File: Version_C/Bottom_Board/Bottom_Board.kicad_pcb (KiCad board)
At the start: 2 copper layers, 74.8 x 84.5 mm, 47 parts, among them J1 Conn_02x03_Top_Bottom, J2 Conn_02x03_Top_Bottom, J3 Screw_Terminal_01x06, J5 DIN-5, SW2 SW_DIP_x04, U1 LM324, U2 LM324

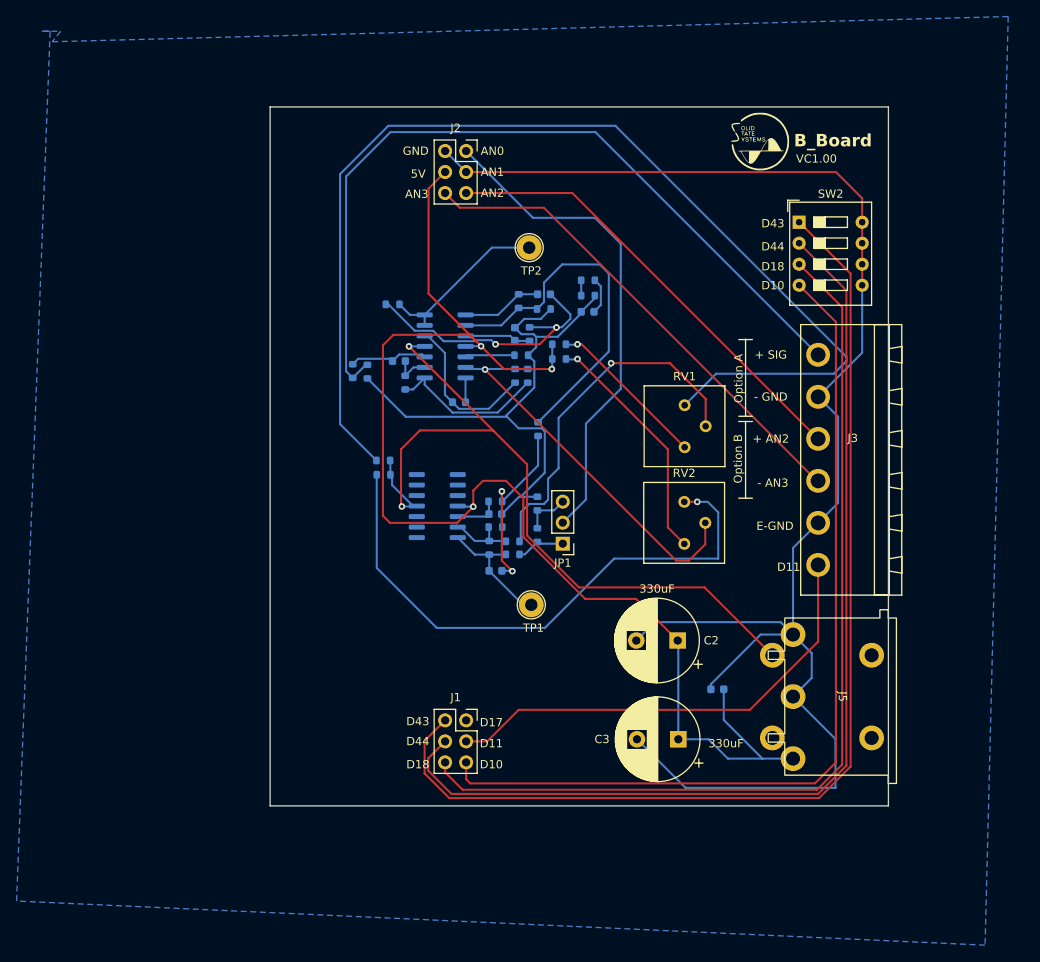
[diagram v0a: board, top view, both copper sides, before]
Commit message: fixed directory overwrite
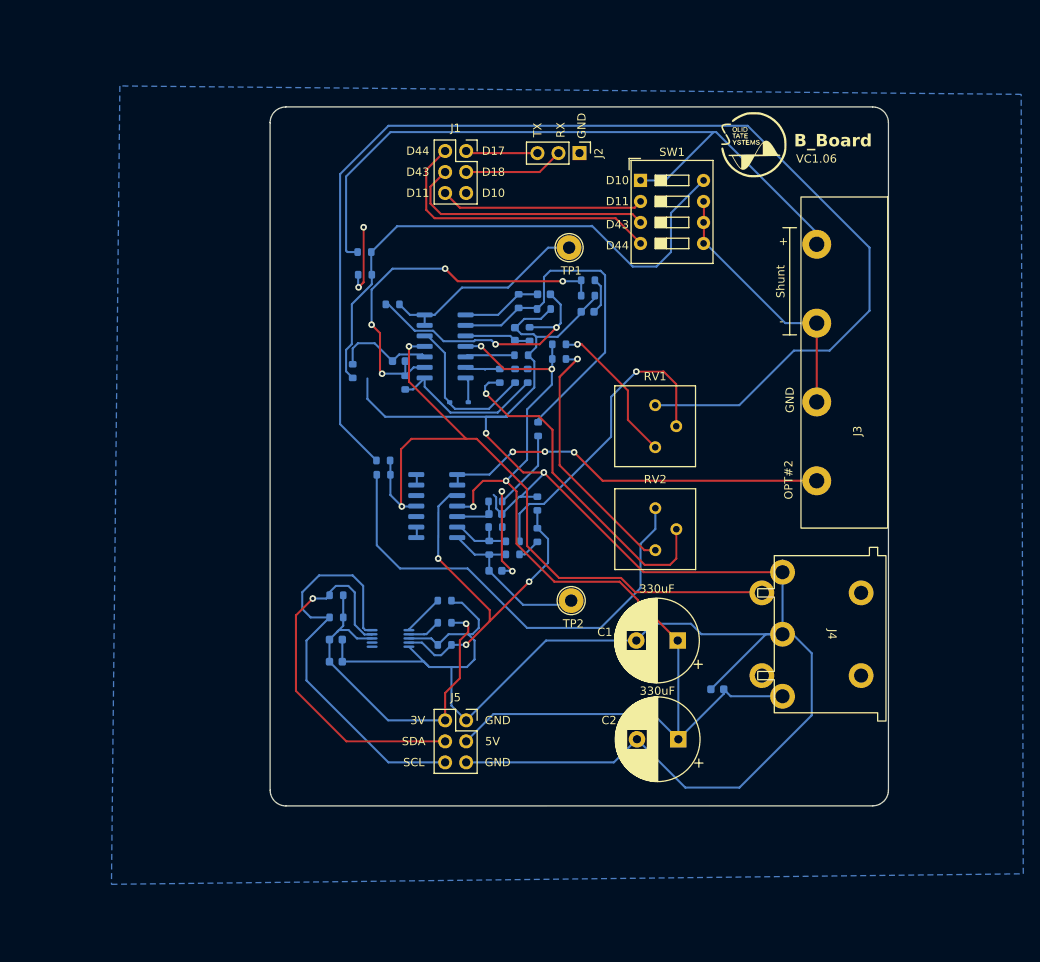
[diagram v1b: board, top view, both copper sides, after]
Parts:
- removed the G*** at (159.3, 67.2)
- removed JP1: Jumper_3_Open, Connector_PinHeader_2.54mm:PinHeader_1x03_P2.54mm_Vertical
- removed the R4 at (111.8, 95.0)
- removed SW2: SW_DIP_x04, Button_Switch_THT:SW_DIP_SPSTx04_Slide_9.78x12.34mm_W7.62mm_P2.54mm
- added C10: 0.1uF, Capacitor_SMD:C_0603_1608Metric, B.Cu at (108.0, 130.1)
- added C9: 1uF, Capacitor_SMD:C_0603_1608Metric, B.Cu at (108.0, 127.4)
- added G***: LOGO, bot_lib:logo_SSS, F.Cu at (158.5, 67.6)
- added G***: LOGO, bot_lib:logo_AN, B.Cu at (104.9, 67.1)
- added J2: Conn_01x03_Pin, Connector_PinHeader_2.54mm:PinHeader_1x03_P2.54mm_Vertical, F.Cu at (137.4, 68.6)
- added R10A1: 20K, Resistor_SMD:R_0603_1608Metric, B.Cu at (111.4, 80.5)
- added R10B1: 20k, Resistor_SMD:R_0603_1608Metric, B.Cu at (111.5, 83.3)
- added R14: 1M, Resistor_SMD:R_0603_1608Metric, B.Cu at (127.8, 95.5)
- added R26: 10K, Resistor_SMD:R_0603_1608Metric, B.Cu at (121.1, 122.7)
- added R27: 10K, Resistor_SMD:R_0603_1608Metric, B.Cu at (108.0, 122.0)
- added R28: 10K, Resistor_SMD:R_0603_1608Metric, B.Cu at (121.1, 125.4)
- added R29: 10K, Resistor_SMD:R_0603_1608Metric, B.Cu at (108.0, 124.7)
- added R30: 3.9M, Resistor_SMD:R_0603_1608Metric, B.Cu at (121.1, 128.0)
- added SW1: SW_DIP_x04, Button_Switch_THT:SW_DIP_SPSTx04_Slide_9.78x12.34mm_W7.62mm_P2.54mm, F.Cu at (144.8, 71.9)
- added U3: ADS1015IDGSR, bot_lib:DGS0010A_N, B.Cu at (114.6, 127.3)
- C11: renamed from C1; value .1uF -> 0.1uF
- C3: renamed from C8; value .1uF -> 0.1uF
- C4: renamed from C7; value 0.1 uF -> 0.1uF
- C5: renamed from C9; value .1uF -> 0.1uF
- C6: renamed from C5; value .002uF -> 0.002uF
- D1: value 1N914 -> 1N4148WS; footprint Diode_SMD:D_0603_1608Metric -> bot_lib:Diode_1N4148WS
- J1: renamed from J2; footprint Connector_PinSocket_2.54mm:PinSocket_2x03_P2.54mm_Vertical -> bot_lib:PinSocket_2x03_P2.54mm_Vertical
- J3: value Screw_Terminal_01x06 -> Screw_Terminal_01x04; footprint Connector_Phoenix_MSTB:PhoenixContact_MSTBA_2,5_6-G-5,08_1x06_P5.08mm_Horizontal -> bot_lib:Terminal_Strip_4_Pin
- J5: renamed from J1; footprint Connector_PinSocket_2.54mm:PinSocket_2x03_P2.54mm_Vertical -> bot_lib:PinSocket_2x03_P2.54mm_Vertical
- RV1, RV2: value 20K -> 20K POT; footprint Potentiometer_THT:Potentiometer_Bourns_3386P_Vertical -> bot_lib:Potentiometer_Bourns_3386P_Vertical
- U1, U2: value LM324 -> LM324DR
- moved J3 10.2 mm to (166.1, 108.2)
- moved J4 7.65 mm to (167.9, 126.7)
- moved TP2 4.85 mm to (136.4, 122.7)
- moved TP1 4.83 mm to (136.1, 80.0)
- moved RV2 3.58 mm to (146.6, 116.6)
- moved RV1 3.56 mm to (146.6, 104.1)
- moved U2 0.06 mm to (120.1, 111.3)
- renumbered C2 to C1, C3 to C2, C6 to C7, C4 to C8, J5 to J4, R10 to R1, R5 to R11, R16 to R12, R19 to R13, R11 to R15, R22 to R16, R3 to R17, R14 to R19, R7 to R2, R1 to R20, R13 to R21, R6 to R22, R9 to R23, R12 to R24, R8 to R25, R24 to R3, R23 to R4, R20 to R5, R2 to R6, R21 to R7, R15 to R8, R17 to R9, TP2 to TP1, TP1 to TP2
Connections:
- net 12V renamed +12V
- net 2x_OUTPUT renamed Net-(R21-Pad2)
- C1 pad 1: 5V -> +5VD
- C1 pad 2: AN1 -> GND
- C11 pad 1: 5V -> +5VD
- C11 pad 2: AN1 -> GND
- C2 pad 1: 5V -> +5VD
- C2 pad 2: AN1 -> GND
- C4 pad 2: E60 -> GND
- C5 pad 2: E60 -> GND
- C7 pad 1: E60 -> GND
- J1 pad 1: AN0 -> TX
- J1 pad 2: AN1 -> D44
- J1 pad 3: AN1 -> RX
- J1 pad 4: 5V -> D43
- J1 pad 5: AN2 -> D10
- J1 pad 6: AN3 -> D11
- J3 pad 1: D11 -> OPT.#2
- J3 pad 2: AN1 -> GND
- J3 pad 3: AN3 -> GND
- J3 pad 4: AN2 -> E23_INPUT
- J4 pad 1: AN1 -> GND
- J4 pad 2: AN1 -> GND
- J4 pad 3: 5V -> +5VD
- J4 pad 6: AN1 -> (no net)
- J4 pad 7: AN1 -> (no net)
- J5 pad 1: D17 -> GND
- J5 pad 2: D43 -> +3V0
- J5 pad 3: D11 -> +5VD
- J5 pad 4: D44 -> SDA
- J5 pad 5: D10 -> GND
- J5 pad 6: D18 -> SCL
- R1 pad 1: Net-(R10-Pad1) -> Net-(U1C--)
- R11 pad 1: E23_INPUT -> SW_OUT
- R19 pad 1: E60 -> GND
- R19 pad 2: 4x_OUTPUT -> AN0
- R2 pad 1: Net-(R10-Pad1) -> Net-(U1C--)
- R2 pad 2: E60 -> GND
- R21 pad 1: 4x_OUTPUT -> AN0
- R23 pad 1: E60 -> GND
- R3 pad 2: E60 -> GND
- R6 pad 2: 5V -> +5VD
- R8 pad 1: 5V -> +5VD
- R9 pad 2: E60 -> GND
- RV2 pad 2: Net-(U1B--) -> Net-(R14-Pad2)
- U1 pad 4: 5V -> +5VD
- U2 pad 1: (no net) -> OPT.#2
- U2 pad 10: (no net) -> GND
- U2 pad 12: (no net) -> GND
- U2 pad 13: (no net) -> Net-(U2D--)
- U2 pad 14: (no net) -> Net-(U2D--)
- U2 pad 2: (no net) -> OPT.#2
- U2 pad 3: (no net) -> AN0
- U2 pad 4: 5V -> +5VD
- U2 pad 8: (no net) -> Net-(U2C--)
- U2 pad 9: (no net) -> Net-(U2C--)
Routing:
- net GND: track 0.00 -> 325.7 mm, vias 0 -> 4
- net AN1: track 193.5 -> 0.00 mm
- net 5V: track 161.7 -> 0.00 mm, vias 3 -> 0
- net +5VD: track 0.00 -> 127.2 mm, vias 0 -> 4
- net D18: track 114.0 -> 0.00 mm
- net D10: track 107.5 -> 0.00 mm
- net D43: track 130.2 -> 30.9 mm
- net D44: track 123.0 -> 35.7 mm
- net E60: track 69.6 -> 0.00 mm
- net SW_OUT: track 0.00 -> 67.5 mm
- net AN3: track 59.5 -> 0.00 mm
- net AN2: track 54.9 -> 0.00 mm
- net SCL: track 0.00 -> 50.4 mm
- net OPT.#2: track 0.00 -> 47.6 mm, vias 0 -> 3
- net SDA: track 0.00 -> 45.3 mm, vias 0 -> 1
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- added copper zone on B.Cu, net GND
- removed copper zone on B.Cu, net AN1
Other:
- outline, holes or cut-outs redrawn
- board text added: "+"
- board text added: "-"
- board text added: "3V"
- board text added: "OPT#2"
- board text added: "RX"
- board text added: "SCL"
- board text added: "SDA"
- board text added: "Shunt"
- board text added: "TX"
- board text added: "VC1.06"
- board text removed: "+ AN2"
- board text removed: "+ SIG"
- board text removed: "- AN3"
- board text removed: "- GND"
- board text removed: "AN0"
- board text removed: "AN1"
- board text removed: "AN2"
- board text removed: "AN3"
- board text removed: "E-GND"
- board text removed: "Feather/LED Width"
- board text removed: "Hardware Filter"
- board text removed: "Option A"
- board text removed: "Option B"
- board text removed: "VC1.00"
